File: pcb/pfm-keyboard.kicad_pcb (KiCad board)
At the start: 2 copper layers, 312.1 x 91 mm, 54 parts, among them U2 ssd1306-display

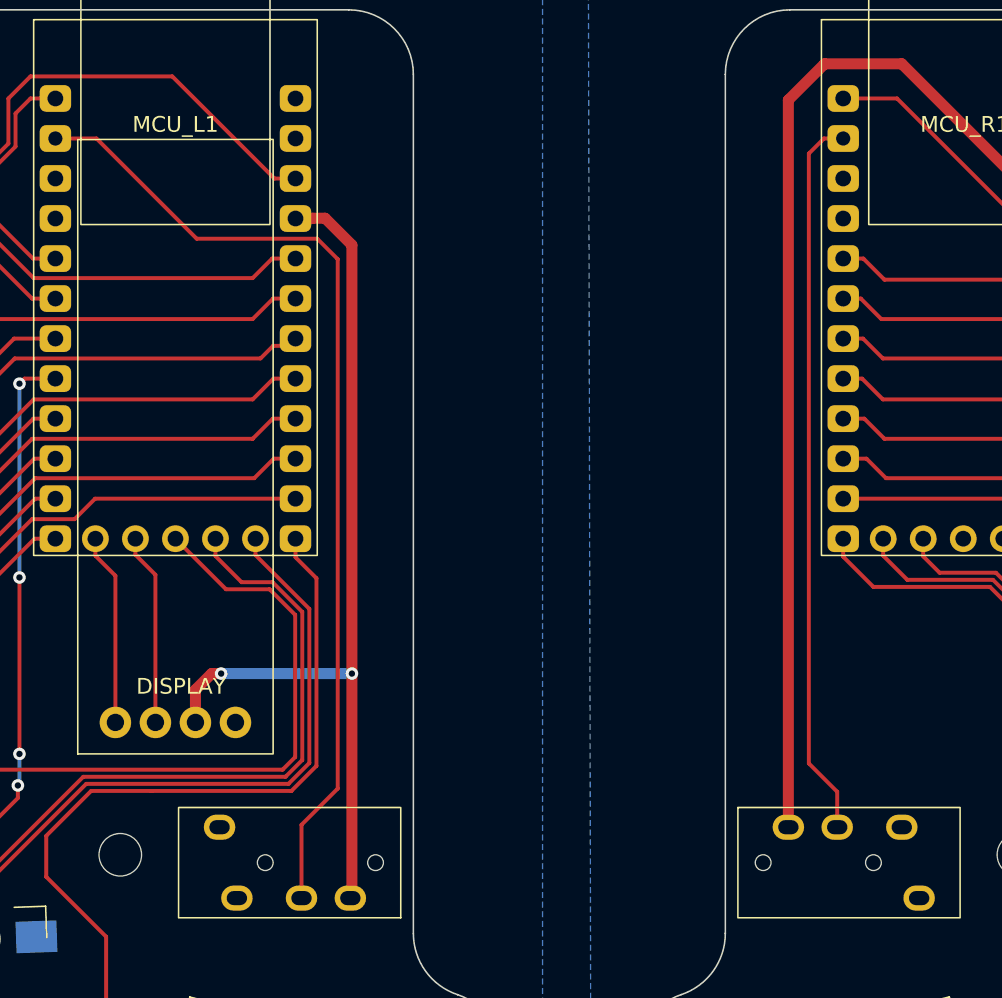
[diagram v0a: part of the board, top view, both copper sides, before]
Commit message: switched connections on TRRS jack for compatibility with TRS cables
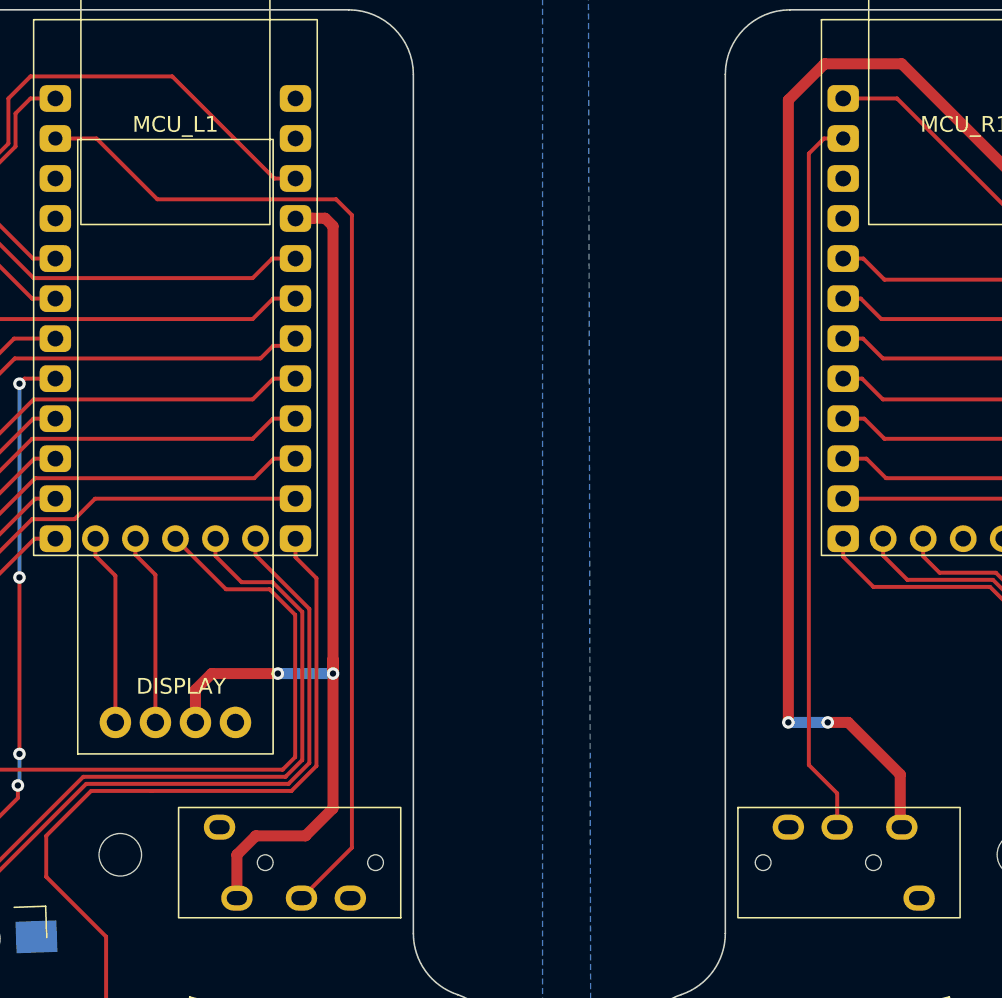
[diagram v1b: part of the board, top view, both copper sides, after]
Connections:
- J_L1 pad R2: VCC_L -> GND_L
- J_L1 pad T: GND_L -> VCC_L
- J_R1 pad R2: VCC_R -> GND_R
- J_R1 pad T: GND_R -> VCC_R
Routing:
- net VCC_R: track 69.9 -> 75.1 mm, vias 0 -> 2
- net VCC_L: track 58.2 -> 61.7 mm
- net LDATA: track 62.6 -> 65.5 mm

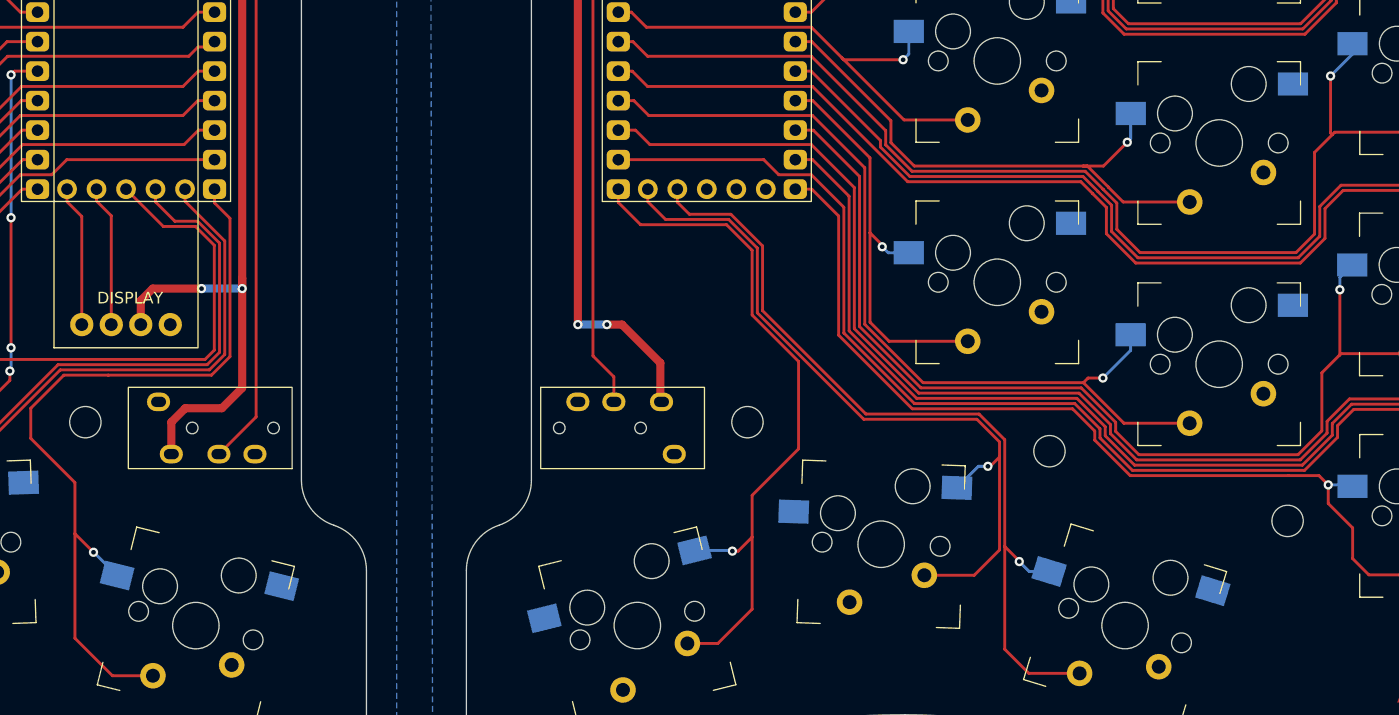
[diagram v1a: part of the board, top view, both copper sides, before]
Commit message: Use same MCU pins on left and right to avoid problems when right is master. Added mounting holes to schematic.
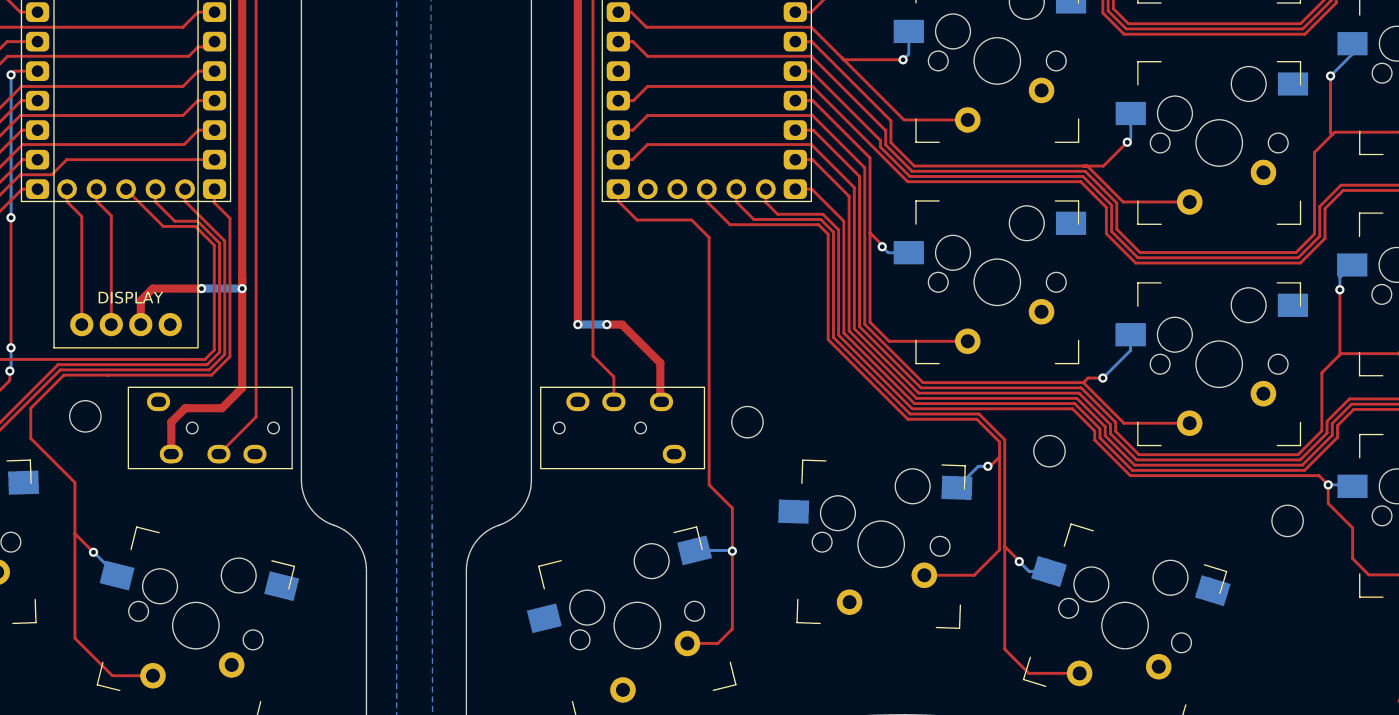
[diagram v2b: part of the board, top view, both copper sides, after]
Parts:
- removed REF** (x8): MountingHole_2.7mm_M2.5, MountingHole:MountingHole_2.7mm_M2.5
- added M_L1: MountingHole, MountingHole:MountingHole_2.7mm_M2.5, F.Cu at (154.4, 37.1)
- added M_L2: MountingHole, MountingHole:MountingHole_2.7mm_M2.5, F.Cu at (166.4, 83.7)
- added M_L3: MountingHole, MountingHole:MountingHole_2.7mm_M2.5, F.Cu at (140.4, 86.7)
- added M_L4: MountingHole, MountingHole:MountingHole_2.7mm_M2.5, F.Cu at (120.0, 92.7)
- added M_R1: MountingHole, MountingHole:MountingHole_2.7mm_M2.5, F.Cu at (235.4, 37.1)
- added M_R2: MountingHole, MountingHole:MountingHole_2.7mm_M2.5, F.Cu at (223.4, 84.2)
- added M_R3: MountingHole, MountingHole:MountingHole_2.7mm_M2.5, F.Cu at (249.4, 86.7)
- added M_R4: MountingHole, MountingHole:MountingHole_2.7mm_M2.5, F.Cu at (269.9, 92.7)
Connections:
- MCU_R1 pad 10: SW_RD3 -> SW_RB3
- MCU_R1 pad 11: SW_RE3 -> SW_RD3
- MCU_R1 pad 13: SW_RC4 -> SW_RE3
- MCU_R1 pad 25: SW_RG2 -> unconnected-(MCU_R1-D12-Pad25)
- MCU_R1 pad 26: SW_RG3 -> unconnected-(MCU_R1-D13-Pad26)
- MCU_R1 pad 27: unconnected-(MCU_R1-D14-Pad27) -> SW_RG2
- MCU_R1 pad 28: unconnected-(MCU_R1-D15-Pad28) -> SW_RG3
- MCU_R1 pad 29: unconnected-(MCU_R1-D16-Pad29) -> SW_RC4
- MCU_R1 pad 8: SW_RE2 -> unconnected-(MCU_R1-D5-Pad8)
- MCU_R1 pad 9: SW_RB3 -> SW_RE2
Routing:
- net SW_RE3: track 148.4 -> 131.4 mm
- net SW_RG1: track 60.8 -> 52.3 mm
- net SW_RG3: track 71.1 -> 68.1 mm
- net SW_RG2: track 64.6 -> 61.6 mm
- net SW_RC4: track 77.9 -> 80.4 mm

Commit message: Version 4 - better key placement, same pin usage on left and right, added test points
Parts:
- added TL1: Conn_01x03_Pin, Connector_PinHeader_2.54mm:PinHeader_1x03_P2.54mm_Vertical, F.Cu at (147.9, 37.6)
- added TR1: Conn_01x03_Pin, Connector_PinHeader_2.54mm:PinHeader_1x03_P2.54mm_Vertical, F.Cu at (241.9, 37.6)
- moved M_L4 54.7 mm to (73.0, 64.7)
- moved M_R4 54.7 mm to (316.9, 64.7)
- moved M_R3 21.5 mm to (269.9, 93.2)
- moved M_L3 21.5 mm to (120.0, 93.2)
- moved SW_LF2 17.0 mm to (49.5, 70.6)
- moved SW_RF1 17.0 mm to (340.5, 70.6)
- moved J_L1 13.7 mm to (171.9, 78.7)
- moved J_R1 13.7 mm to (217.9, 78.7)
- moved M_L1 13.6 mm to (140.9, 38.6)
- moved M_R1 13.6 mm to (248.9, 38.6)
- moved M_R2 13.3 mm to (227.9, 71.7)
- moved M_L2 12.8 mm to (161.9, 71.7)
- moved U2 10.3 mm to (167.9, 65.7)
- moved SW_LE1 9.02 mm to (68.5, 52.5)
- moved SW_RE1 9.01 mm to (321.3, 52.6)
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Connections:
- MCU_L1 pad 10: SW_LB3 -> SW_LA2
- MCU_L1 pad 11: SW_LD3 -> SW_LC3
- MCU_L1 pad 13: SW_LG1 -> SW_LC4
- MCU_L1 pad 14: SW_LF1 -> SW_LD3
- MCU_L1 pad 15: SW_LC3 -> SW_LB3
- MCU_L1 pad 16: SW_LA2 -> SW_LE2
- MCU_L1 pad 17: SW_LD2 -> SW_LC2
- MCU_L1 pad 18: SW_LC2 -> SW_LA1
- MCU_L1 pad 19: SW_LA1 -> SW_LE1
- MCU_L1 pad 20: SW_LD1 -> SW_LC1
- MCU_L1 pad 27: SW_LC4 -> SW_LG1
- MCU_L1 pad 28: SW_LG3 -> SW_LG2
- MCU_L1 pad 29: SW_LG2 -> SW_LG3
- MCU_L1 pad 5: SW_LC1 -> SW_LD1
- MCU_L1 pad 6: SW_LE1 -> SW_LF1
- MCU_L1 pad 9: SW_LE2 -> SW_LD2
- MCU_R1 pad 10: SW_RB3 -> SW_RA2
- MCU_R1 pad 11: SW_RD3 -> SW_RC3
- MCU_R1 pad 12: SW_RG1 -> SW_RE3
- MCU_R1 pad 13: SW_RE3 -> SW_RC4
- MCU_R1 pad 14: SW_RF1 -> SW_RD3
- MCU_R1 pad 15: SW_RC3 -> SW_RB3
- MCU_R1 pad 16: SW_RA2 -> SW_RE2
- MCU_R1 pad 17: SW_RD2 -> SW_RC2
- MCU_R1 pad 18: SW_RB2 -> SW_RA1
- MCU_R1 pad 27: SW_RG2 -> SW_RG1
- MCU_R1 pad 28: SW_RG3 -> SW_RG2
- MCU_R1 pad 29: SW_RC4 -> SW_RG3
- MCU_R1 pad 6: SW_RA1 -> SW_RF1
- MCU_R1 pad 7: SW_RC2 -> SW_RB2
- MCU_R1 pad 9: SW_RE2 -> SW_RD2
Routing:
- net RDATA: track 46.1 -> 73.1 mm, vias 0 -> 4
- net SW_LF1: track 164.9 -> 139.3 mm
- net SW_RB2: track 48.0 -> 69.9 mm
- net SW_RC3: track 87.4 -> 109.2 mm
- net SW_RA2: track 35.8 -> 57.1 mm
- net SW_LD1: track 106.5 -> 86.0 mm
- net SW_RD2: track 93.7 -> 113.9 mm
- net SW_RE3: track 131.4 -> 150.9 mm
- net LDATA: track 65.5 -> 83.6 mm, vias 0 -> 1
- net SW_LD3: track 101.1 -> 118.9 mm
- net SW_LB3: track 60.4 -> 78.0 mm
- net SW_LE2: track 119.9 -> 136.7 mm
- net VCC_L: track 61.7 -> 78.1 mm
- net VCC_R: track 75.1 -> 90.8 mm, vias 2 -> 1
- net SW_RG1: track 52.3 -> 67.9 mm
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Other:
- board size 312.1 x 91 mm -> 314.1 x 97.8 mm
